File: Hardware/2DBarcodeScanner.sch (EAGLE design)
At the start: 36 parts, among them Q1 600mA/40V, Q2 600mA/40V, U1 3.3V

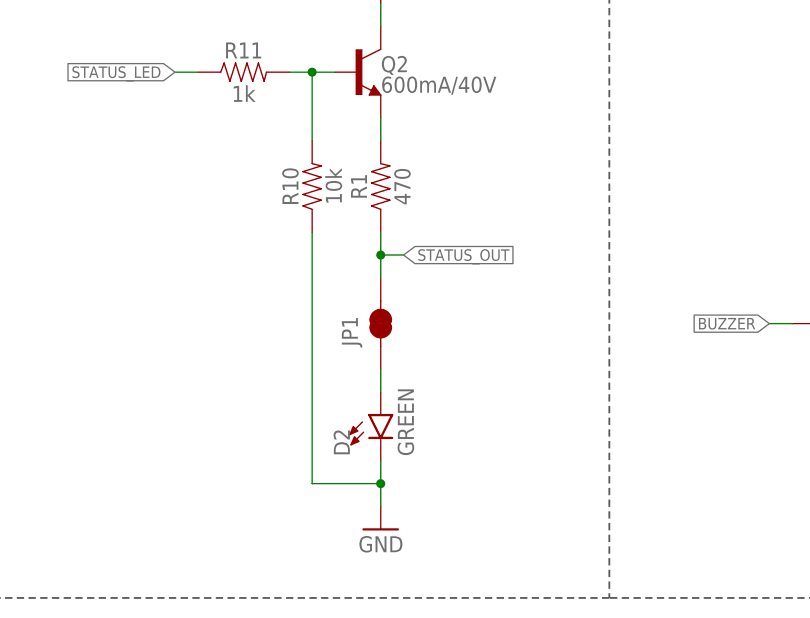
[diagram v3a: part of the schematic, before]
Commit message: Change out green stat LED for yellow
Pull-up resistor 470 --> 1k ohm
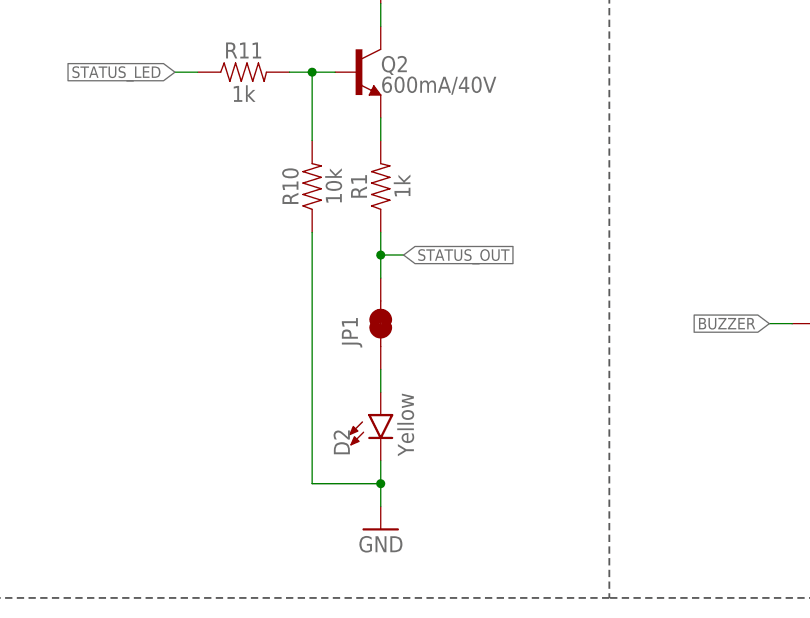
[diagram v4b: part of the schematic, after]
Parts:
- D2: value GREEN -> Yellow; device SparkFun-LED:LED-GREEN0603 -> SparkFun-LED:LED-YELLOW0603
- R1: value 470 -> 1k; device SparkFun-Resistors:470OHM-0603-1/10W-1% -> SparkFun-Resistors:1KOHM-0603-1/10W-1%
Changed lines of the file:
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@@
 <part name="GND10" library="SparkFun-PowerSymbols" deviceset="GND" device=""/>
 <part name="SUPPLY6" library="SparkFun-PowerSymbols" deviceset="3.3V" device=""/>
-<part name="D2" library="SparkFun-LED" deviceset="LED-GREEN" device="0603" value="GREEN"/>
 <part name="C3" library="SparkFun-Capacitors" deviceset="0.1UF" device="-0603-25V-(+80/-20%)" value="0.1uF"/>
 <part name="GND13" library="SparkFun-PowerSymbols" deviceset="GND" device=""/>
@@
 <part name="S2" library="SparkFun-Switches" deviceset="MOMENTARY-SWITCH-SPST" device="-SMD-5.2MM-TALL"/>
 <part name="FRAME1" library="SparkFun-Aesthetics" deviceset="FRAME-LETTER" device="NO_PACKAGE"/>
-<part name="R1" library="SparkFun-Resistors" deviceset="470OHM" device="-0603-1/10W-1%" value="470"/>
 <part name="J4" library="SparkFun-Connectors" deviceset="CONN_06" device="NO_SILK_FEMALE_PTH"/>
 <part name="JP1" library="SparkFun-Jumpers" deviceset="JUMPER-SMT_2_NC_TRACE" device="_SILK" package3d_urn="urn:adsk.eagle:package:39281/1"/>
@@
 <part name="GND12" library="SparkFun-PowerSymbols" deviceset="GND" device=""/>
 <part name="SUPPLY2" library="SparkFun-PowerSymbols" deviceset="3.3V" device=""/>
+<part name="D2" library="SparkFun-LED" deviceset="LED-YELLOW" device="0603" value="Yellow"/>
+<part name="R1" library="SparkFun-Resistors" deviceset="1KOHM" device="-0603-1/10W-1%" value="1k"/>
 </parts>
 <sheets>
@@
 <attribute name="VALUE" x="50.8" y="104.394" size="1.778" layer="96" font="vector" align="bottom-center"/>
 </instance>
-<instance part="D2" gate="G$1" x="50.8" y="55.88" smashed="yes">
-<attribute name="NAME" x="47.371" y="51.308" size="1.778" layer="95" font="vector" rot="R90"/>
-<attribute name="VALUE" x="52.705" y="51.308" size="1.778" layer="96" font="vector" rot="R90" align="top-left"/>
-</instance>
 <instance part="C3" gate="G$1" x="208.28" y="60.96" smashed="yes" rot="MR0">
 <attribute name="NAME" x="211.836" y="63.881" size="1.778" layer="95" font="vector" rot="MR0"/>
@@
 <attribute name="SHEET" x="233.68" y="1.27" size="2.54" layer="94" font="vector"/>
 <attribute name="DRAWING_NAME" x="162.814" y="17.78" size="2.7432" layer="94" font="vector"/>
-</instance>
-<instance part="R1" gate="G$1" x="50.8" y="81.28" smashed="yes" rot="R90">
-<attribute name="NAME" x="49.276" y="81.28" size="1.778" layer="95" font="vector" rot="R90" align="bottom-center"/>
-<attribute name="VALUE" x="52.324" y="81.28" size="1.778" layer="96" font="vector" rot="R90" align="top-center"/>
 </instance>
 <instance part="J4" gate="G$1" x="175.26" y="154.94" smashed="yes">
@@
 <instance part="SUPPLY2" gate="G$1" x="193.04" y="104.14" smashed="yes">
 <attribute name="VALUE" x="193.04" y="106.934" size="1.778" layer="96" align="bottom-center"/>
+</instance>
+<instance part="D2" gate="G$1" x="50.8" y="55.88" smashed="yes">
+<attribute name="NAME" x="47.371" y="51.308" size="1.778" layer="95" font="vector" rot="R90"/>
+<attribute name="VALUE" x="52.705" y="51.308" size="1.778" layer="96" font="vector" rot="R90" align="top-left"/>
+</instance>
+<instance part="R1" gate="G$1" x="50.8" y="81.28" smashed="yes" rot="R90">
+<attribute name="NAME" x="49.276" y="81.28" size="1.778" layer="95" font="vector" rot="R90" align="bottom-center"/>
+<attribute name="VALUE" x="52.324" y="81.28" size="1.778" layer="96" font="vector" rot="R90" align="top-center"/>
 </instance>
 </instances>
@@
 </segment>
 <segment>
-<pinref part="D2" gate="G$1" pin="C"/>
 <pinref part="GND10" gate="1" pin="GND"/>
 <wire x1="50.8" y1="45.72" x2="50.8" y2="48.26" width="0.1524" layer="91"/>
@@
 <wire x1="43.18" y1="48.26" x2="50.8" y2="48.26" width="0.1524" layer="91"/>
 <junction x="50.8" y="48.26"/>
+<pinref part="D2" gate="G$1" pin="C"/>
 </segment>
 <segment>
@@
 <net name="STATUS_OUT" class="0">
 <segment>
-<pinref part="R1" gate="G$1" pin="1"/>
 <pinref part="JP1" gate="G$1" pin="2"/>
 <wire x1="50.8" y1="76.2" x2="50.8" y2="73.66" width="0.1524" layer="91"/>
@@
 <junction x="50.8" y="73.66"/>
 <label x="53.34" y="73.66" size="1.27" layer="95" xref="yes"/>
+<pinref part="R1" gate="G$1" pin="1"/>
 </segment>
 <segment>
@@
 <segment>
 <pinref part="JP1" gate="G$1" pin="1"/>
+<wire x1="50.8" y1="60.96" x2="50.8" y2="58.42" width="0.1524" layer="91"/>
 <pinref part="D2" gate="G$1" pin="A"/>
-<wire x1="50.8" y1="60.96" x2="50.8" y2="58.42" width="0.1524" layer="91"/>
-</segment>
-</net>
+</segment>
+</net>

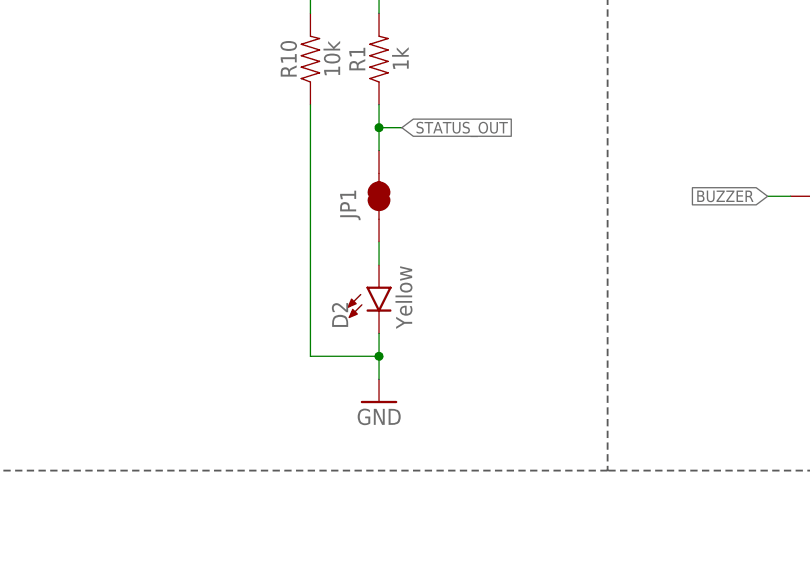
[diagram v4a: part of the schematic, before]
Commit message: Switch yellow stat LED out for blue
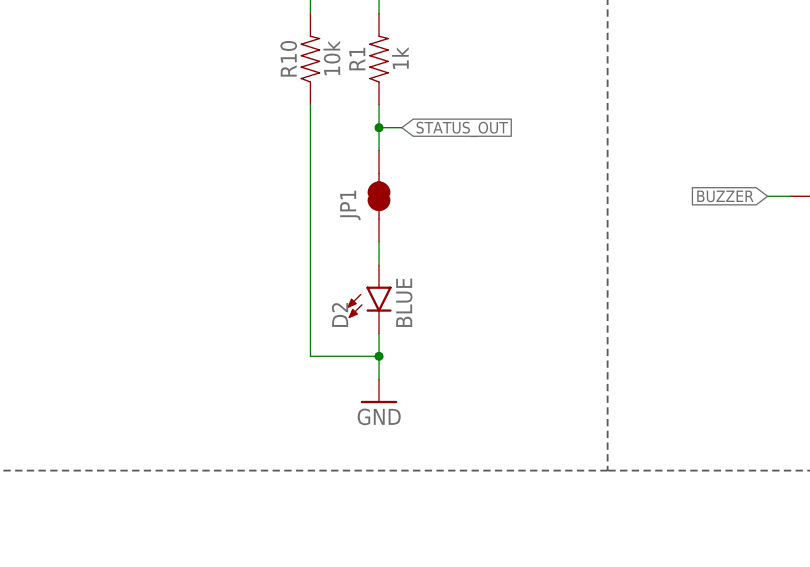
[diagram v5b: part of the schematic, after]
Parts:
- D2: value Yellow -> BLUE; device SparkFun-LED:LED-YELLOW0603 -> SparkFun-LED:LED-BLUE0603
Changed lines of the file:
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@@
 <part name="GND12" library="SparkFun-PowerSymbols" deviceset="GND" device=""/>
 <part name="SUPPLY2" library="SparkFun-PowerSymbols" deviceset="3.3V" device=""/>
-<part name="D2" library="SparkFun-LED" deviceset="LED-YELLOW" device="0603" value="Yellow"/>
 <part name="R1" library="SparkFun-Resistors" deviceset="1KOHM" device="-0603-1/10W-1%" value="1k"/>
+<part name="D2" library="SparkFun-LED" deviceset="LED-BLUE" device="0603" value="BLUE"/>
 </parts>
 <sheets>
@@
 <attribute name="VALUE" x="193.04" y="106.934" size="1.778" layer="96" align="bottom-center"/>
 </instance>
+<instance part="R1" gate="G$1" x="50.8" y="81.28" smashed="yes" rot="R90">
+<attribute name="NAME" x="49.276" y="81.28" size="1.778" layer="95" font="vector" rot="R90" align="bottom-center"/>
+<attribute name="VALUE" x="52.324" y="81.28" size="1.778" layer="96" font="vector" rot="R90" align="top-center"/>
+</instance>
 <instance part="D2" gate="G$1" x="50.8" y="55.88" smashed="yes">
 <attribute name="NAME" x="47.371" y="51.308" size="1.778" layer="95" font="vector" rot="R90"/>
 <attribute name="VALUE" x="52.705" y="51.308" size="1.778" layer="96" font="vector" rot="R90" align="top-left"/>
 </instance>
-<instance part="R1" gate="G$1" x="50.8" y="81.28" smashed="yes" rot="R90">
-<attribute name="NAME" x="49.276" y="81.28" size="1.778" layer="95" font="vector" rot="R90" align="bottom-center"/>
-<attribute name="VALUE" x="52.324" y="81.28" size="1.778" layer="96" font="vector" rot="R90" align="top-center"/>
-</instance>
 </instances>

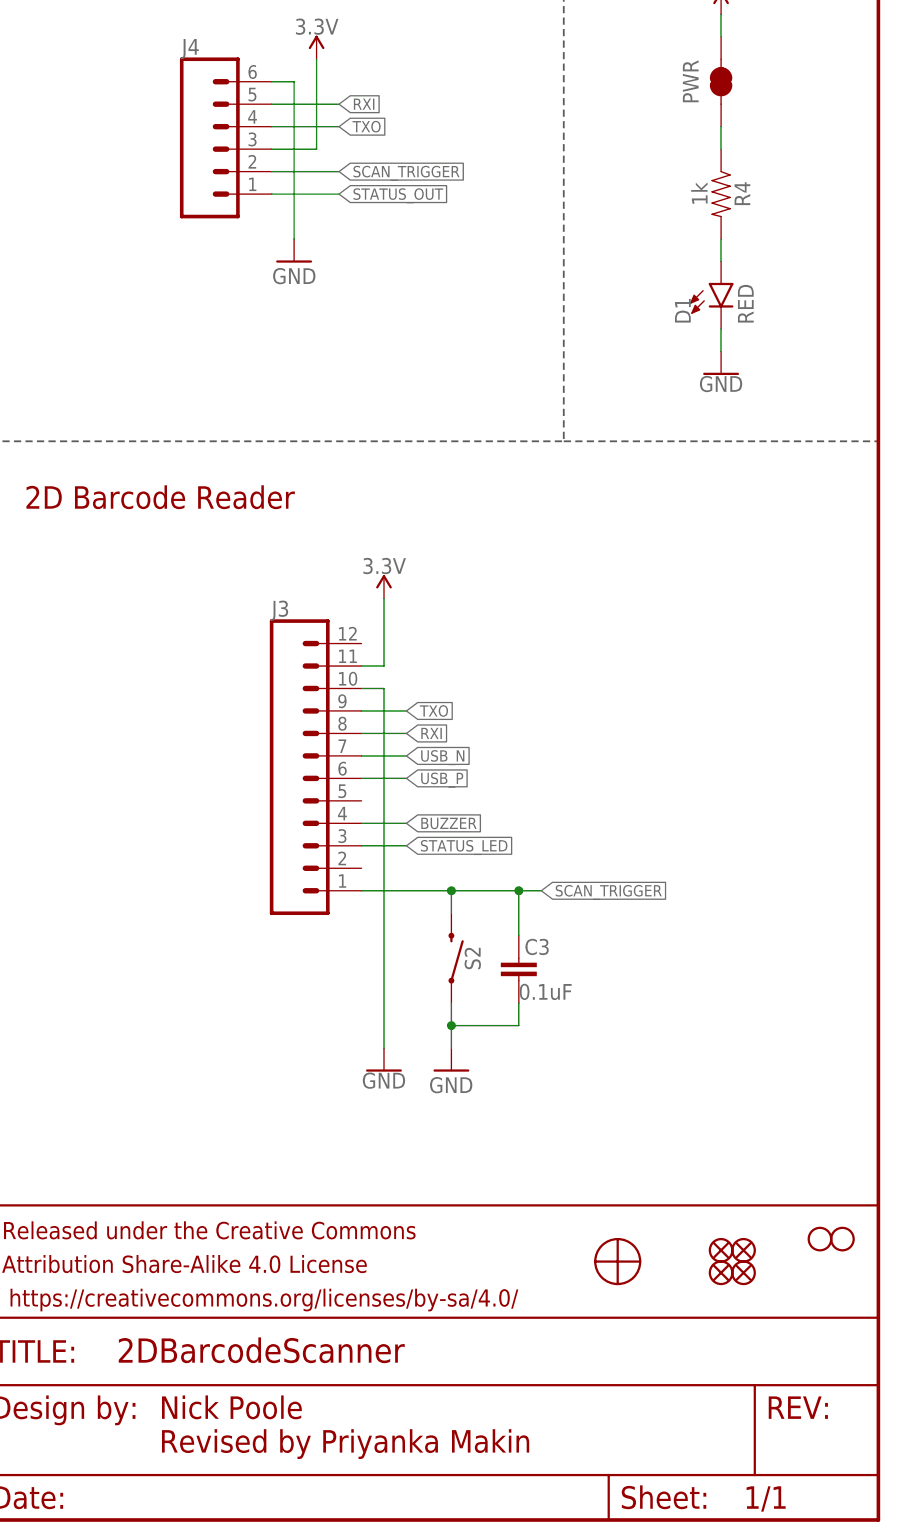
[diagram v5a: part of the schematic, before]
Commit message: Design Review Changes
Update schematic frame
Dimension width 0.008
Increased width of GND polygon
Moved v10 label on bottom
Moved bottom jumpers in-line
Added measures
Made y-axis of board 1-in, mounting holes on 0.8in
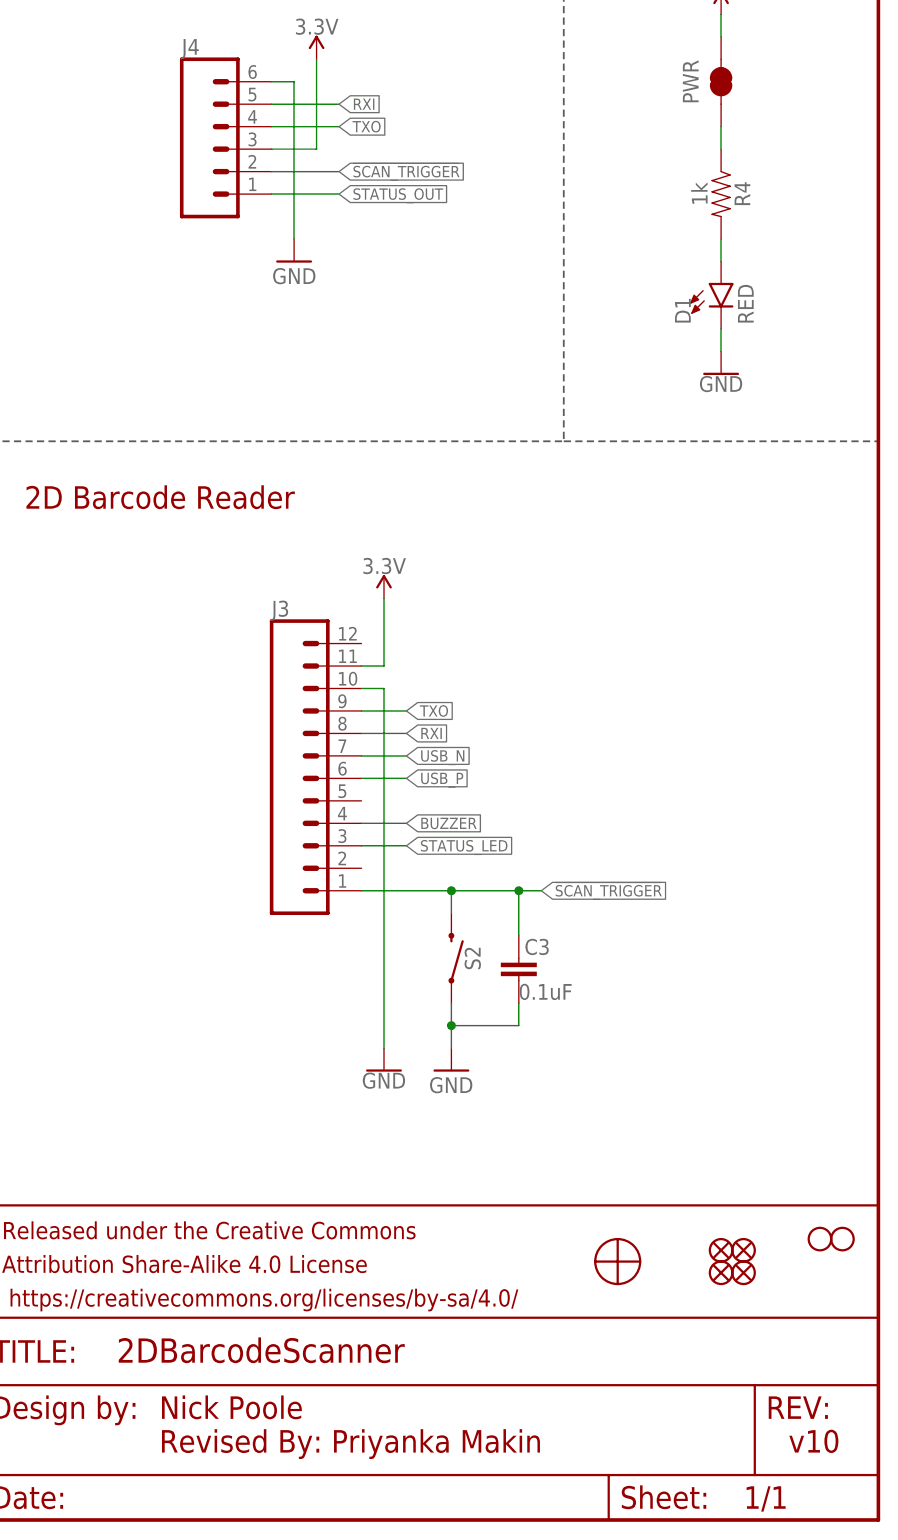
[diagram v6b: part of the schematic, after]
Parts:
- FRAME1: value FRAME-LETTERNO_PACKAGE -> FRAME-LETTER; device SparkFun-Aesthetics:FRAME-LETTERNO_PACKAGE -> SparkFun-Aesthetics:FRAME-LETTER
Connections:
- net SCAN_TRIGGER renamed !SCAN_TRIGGER!
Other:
- note added: "Nick Poole Revised By: Priyanka Makin"
- note added: "v10"
- note removed: "Nick Poole Revised by Priyanka Makin"
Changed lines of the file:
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@@
 <part name="H3" library="SparkFun-Hardware" deviceset="STAND-OFF" device=""/>
 <part name="S2" library="SparkFun-Switches" deviceset="MOMENTARY-SWITCH-SPST" device="-SMD-5.2MM-TALL"/>
-<part name="FRAME1" library="SparkFun-Aesthetics" deviceset="FRAME-LETTER" device="NO_PACKAGE"/>
 <part name="J4" library="SparkFun-Connectors" deviceset="CONN_06" device="NO_SILK_FEMALE_PTH"/>
 <part name="JP1" library="SparkFun-Jumpers" deviceset="JUMPER-SMT_2_NC_TRACE" device="_SILK" package3d_urn="urn:adsk.eagle:package:39281/1"/>
@@
 <part name="R1" library="SparkFun-Resistors" deviceset="1KOHM" device="-0603-1/10W-1%" value="1k"/>
 <part name="D2" library="SparkFun-LED" deviceset="LED-BLUE" device="0603" value="BLUE"/>
+<part name="FRAME1" library="SparkFun-Aesthetics" deviceset="FRAME-LETTER" device=""/>
 </parts>
 <sheets>
@@
 <wire x1="76.2" y1="121.92" x2="76.2" y2="185.42" width="0.2032" layer="97" style="longdash"/>
 <wire x1="147.32" y1="121.92" x2="147.32" y2="185.42" width="0.2032" layer="97" style="longdash"/>
-<text x="167.64" y="7.62" size="2.54" layer="94" font="vector">Nick Poole
-Revised by Priyanka Makin</text>
 <wire x1="213.36" y1="185.42" x2="213.36" y2="121.92" width="0.2032" layer="97" style="longdash"/>
 <text x="215.9" y="177.8" size="2.54" layer="94" font="vector">Power LED</text>
+<text x="167.64" y="7.62" size="2.54" layer="94" font="vector">Nick Poole
+Revised By: Priyanka Makin</text>
+<text x="238.76" y="7.62" size="2.54" layer="94" font="vector">v10</text>
 </plain>
 <instances>
@@
 <attribute name="NAME" x="202.184" y="63.5" size="1.778" layer="95" font="vector" rot="MR90" align="bottom-center"/>
 </instance>
-<instance part="FRAME1" gate="G$1" x="0" y="0" smashed="yes"/>
-<instance part="FRAME1" gate="V" x="147.32" y="0" smashed="yes">
-<attribute name="LAST_DATE_TIME" x="160.02" y="1.27" size="2.54" layer="94" font="vector"/>
-<attribute name="SHEET" x="233.68" y="1.27" size="2.54" layer="94" font="vector"/>
-<attribute name="DRAWING_NAME" x="162.814" y="17.78" size="2.7432" layer="94" font="vector"/>
-</instance>
 <instance part="J4" gate="G$1" x="175.26" y="154.94" smashed="yes">
 <attribute name="VALUE" x="170.18" y="145.034" size="1.778" layer="96" font="vector"/>
@@
 <attribute name="NAME" x="47.371" y="51.308" size="1.778" layer="95" font="vector" rot="R90"/>
 <attribute name="VALUE" x="52.705" y="51.308" size="1.778" layer="96" font="vector" rot="R90" align="top-left"/>
+</instance>
+<instance part="FRAME1" gate="G$1" x="0" y="0" smashed="yes"/>
+<instance part="FRAME1" gate="V" x="147.32" y="0" smashed="yes">
+<attribute name="LAST_DATE_TIME" x="160.02" y="1.27" size="2.54" layer="94" font="vector"/>
+<attribute name="SHEET" x="233.68" y="1.27" size="2.54" layer="94" font="vector"/>
+<attribute name="DRAWING_NAME" x="162.814" y="17.78" size="2.7432" layer="94" font="vector"/>
+<attribute name="DESIGNER" x="170.434" y="11.176" size="2.7432" layer="94" font="vector"/>
+<attribute name="REV" x="236.22" y="6.604" size="2.7432" layer="94" font="vector"/>
 </instance>
 </instances>
@@
 </segment>
 </net>
-<net name="SCAN_TRIGGER" class="0">
+<net name="!SCAN_TRIGGER!" class="0">
 <segment>
 <wire x1="200.66" y1="71.12" x2="200.66" y2="68.58" width="0.1524" layer="91"/>

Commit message: QC Double Check Changes
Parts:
- renumbered JP1 to PWR_LED, U$1 to U2
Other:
- note added: "Vin Range: 2.5 - 6.0 V"
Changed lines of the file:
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@@
 </classes>
 <parts>
-<part name="U$1" library="SparkFun-Hardware" deviceset="BARCODE_SCANNER_MOUNT" device=""/>
+<part name="U2" library="SparkFun-Hardware" deviceset="BARCODE_SCANNER_MOUNT" device=""/>
 <part name="J2" library="SparkFun-Connectors" deviceset="USB_C" device="_2-LAYER_PADS"/>
 <part name="GND5" library="SparkFun-PowerSymbols" deviceset="GND" device=""/>
@@
 <part name="S2" library="SparkFun-Switches" deviceset="MOMENTARY-SWITCH-SPST" device="-SMD-5.2MM-TALL"/>
 <part name="J4" library="SparkFun-Connectors" deviceset="CONN_06" device="NO_SILK_FEMALE_PTH"/>
-<part name="JP1" library="SparkFun-Jumpers" deviceset="JUMPER-SMT_2_NC_TRACE" device="_SILK" package3d_urn="urn:adsk.eagle:package:39281/1"/>
+<part name="PWR_LED" library="SparkFun-Jumpers" deviceset="JUMPER-SMT_2_NC_TRACE" device="_SILK" package3d_urn="urn:adsk.eagle:package:39281/1"/>
 <part name="FD1" library="SparkFun-Aesthetics" deviceset="FIDUCIAL" device="UFIDUCIAL"/>
 <part name="FD2" library="SparkFun-Aesthetics" deviceset="FIDUCIAL" device="UFIDUCIAL"/>
@@
 Revised By: Priyanka Makin</text>
 <text x="238.76" y="7.62" size="2.54" layer="94" font="vector">v10</text>
+<text x="27.94" y="129.54" size="1.778" layer="94" font="vector">Vin Range: 2.5 - 6.0 V</text>
 </plain>
 <instances>
-<instance part="U$1" gate="G$1" x="219.456" y="29.21" smashed="yes"/>
+<instance part="U2" gate="G$1" x="219.456" y="29.21" smashed="yes"/>
 <instance part="J2" gate="J1" x="93.98" y="154.94" smashed="yes">
 <attribute name="VALUE" x="91.44" y="142.494" size="1.778" layer="96" font="vector" rot="MR180" align="top-left"/>
@@
 <attribute name="NAME" x="170.18" y="165.608" size="1.778" layer="95" font="vector"/>
 </instance>
-<instance part="JP1" gate="G$1" x="50.8" y="66.04" smashed="yes" rot="R90">
+<instance part="PWR_LED" gate="G$1" x="50.8" y="66.04" smashed="yes" rot="R90">
 <attribute name="NAME" x="48.26" y="63.5" size="1.778" layer="95" font="vector" rot="R90"/>
 </instance>
@@
 <net name="STATUS_OUT" class="0">
 <segment>
-<pinref part="JP1" gate="G$1" pin="2"/>
+<pinref part="PWR_LED" gate="G$1" pin="2"/>
 <wire x1="50.8" y1="76.2" x2="50.8" y2="73.66" width="0.1524" layer="91"/>
 <wire x1="50.8" y1="73.66" x2="50.8" y2="71.12" width="0.1524" layer="91"/>
@@
 <net name="N$8" class="0">
 <segment>
-<pinref part="JP1" gate="G$1" pin="1"/>
+<pinref part="PWR_LED" gate="G$1" pin="1"/>
 <wire x1="50.8" y1="60.96" x2="50.8" y2="58.42" width="0.1524" layer="91"/>
 <pinref part="D2" gate="G$1" pin="A"/>
